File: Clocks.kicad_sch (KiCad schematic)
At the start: 11 parts, among them U3 LMK1C1106A, Y2 O 16,0-JT22CT-A-P-3,3-LF

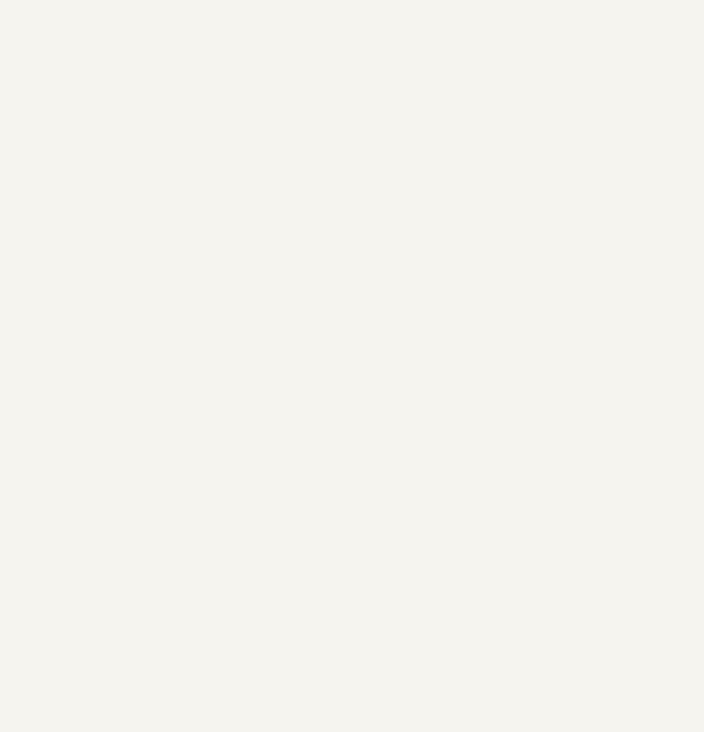
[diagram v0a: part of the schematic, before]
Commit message: Added a thermsistor by the oscillator
For general temperature and for frequency compensation.

Signed-off-by: Corey Minyard <corey@minyard.net>
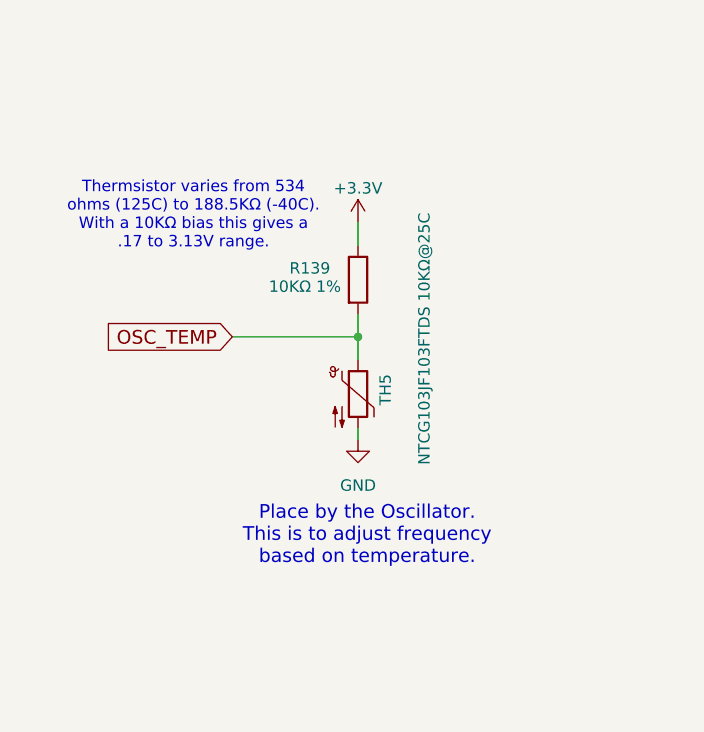
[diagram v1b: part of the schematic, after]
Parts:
- added R139: 10KΩ 1%, Resistor_SMD:R_0402_1005Metric_Pad0.72x0.64mm_HandSolder, symbol Device:R
- added TH5: NTCG103JF103FTDS 10KΩ@25C, Resistor_SMD:R_0402_1005Metric, symbol Device:Thermistor_NTC
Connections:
- net +3.3V: now also R139.1
- net GND: now also TH5.2
- new net OSC_TEMP: R139.2, TH5.1
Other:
- note added: "Place by the Oscillator. This is to adjust frequency based on temperature."
- note added: "Thermsistor varies from 534 ohms (125C) to 188.5KΩ (-40C). With a 10KΩ bias this gives a .17 to 3.13V range."

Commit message: Add a note about a thermal pad on U3
The U3 footprint has a ground pad but the chip itself does not.  Add a
note to put a thermal pad on this chip.

Signed-off-by: Corey Minyard <corey@minyard.net>
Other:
- note added: "This chip does not have a thermal pad on the chip, but does have one in the footprint. Add a thermal pad underneath it to conduct heat from the chip to the board."
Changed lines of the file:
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@@
 		(comment 1 "N5BRG")
+	)
+	(text "This chip does not have a thermal pad on the\nchip, but does have one in the footprint.\nAdd a thermal pad underneath it to conduct\nheat from the chip to the board."
+		(exclude_from_sim no)
+		(at 216.154 149.352 0)
+		(effects
+			(font
+				(size 1.524 1.524)
+			)
+		)
 	)
 	(text "Thermsistor varies from 534\nohms (125C) to 188.5KΩ (-40C).\nWith a 10KΩ bias this gives a\n.17 to 3.13V range."
@@
 	(text "AX5043s have capacitive termination\nat the end of the clocks per their\ndata sheet.  Only need series\ntermination on the CPU clock."
 		(exclude_from_sim no)
-		(at 248.412 134.874 0)
+		(at 285.242 111.506 0)
 		(effects
 			(font

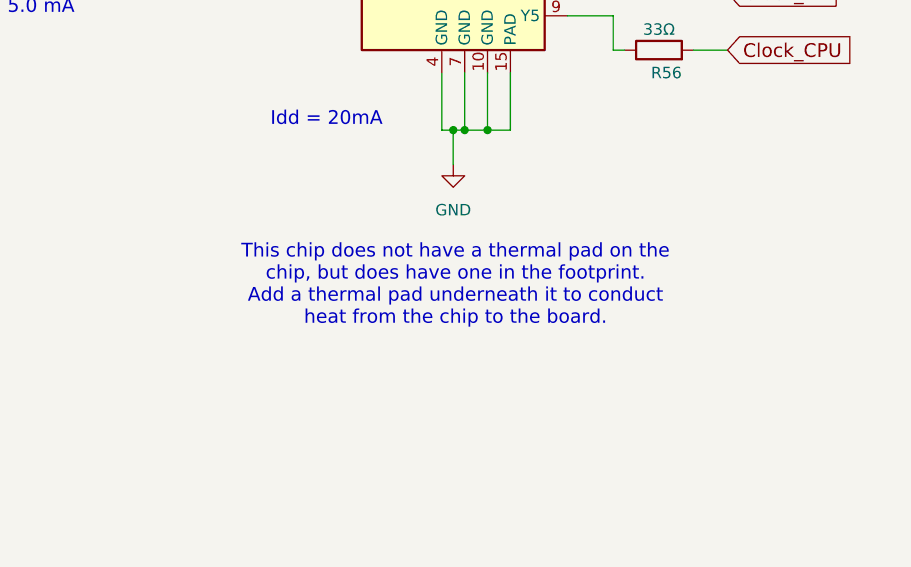
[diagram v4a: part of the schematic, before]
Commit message: Change thermal pads to just be solder contact with the chip
Thermal pads add manufacturing issues and outgassing questions.  I think
the original intent for the clock chip was just to have solder there in
contact with the chip.

So update for that.  This required moving some vias around under the
CPU, but it was doable.

Signed-off-by: Corey Minyard <corey@minyard.net>
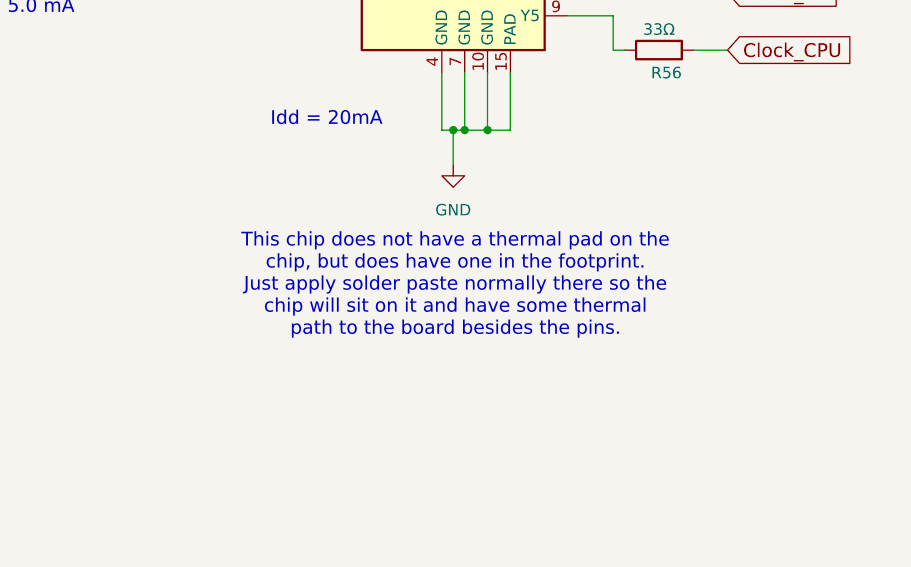
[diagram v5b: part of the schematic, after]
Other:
- note added: "This chip does not have a thermal pad on the chip, but does have one in the footprint. Just apply solder paste normally there so the chip will sit on it and have some thermal path to the board besides the pins."
- note removed: "This chip does not have a thermal pad on the chip, but does have one in the footprint. Add a thermal pad underneath it to conduct heat from the chip to the board."
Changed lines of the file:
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@@
 		(comment 1 "N5BRG")
 	)
-	(text "This chip does not have a thermal pad on the\nchip, but does have one in the footprint.\nAdd a thermal pad underneath it to conduct\nheat from the chip to the board."
+	(text "This chip does not have a thermal pad on the\nchip, but does have one in the footprint.\nJust apply solder paste normally there so the\nchip will sit on it and have some thermal\npath to the board besides the pins."
 		(exclude_from_sim no)
 		(at 216.154 149.352 0)

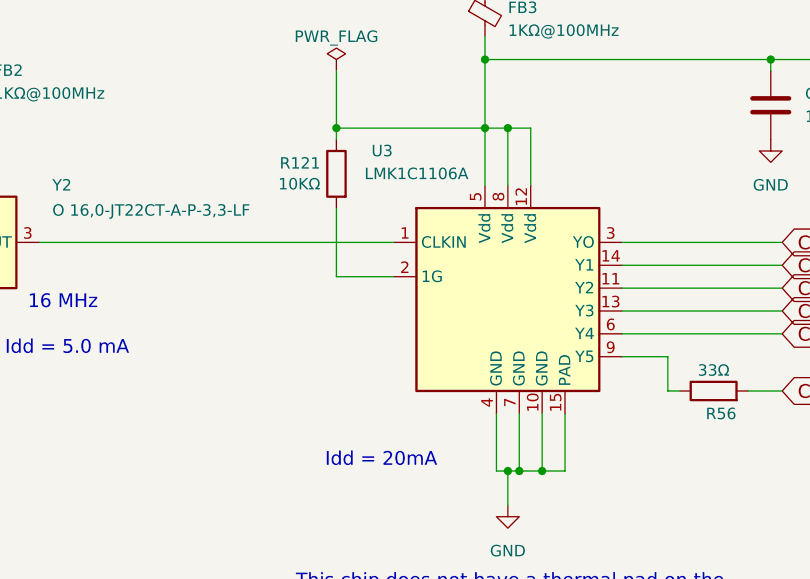
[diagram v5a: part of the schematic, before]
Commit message: Change the LMK1C1106A to a LMK1C1106-Q1
Switch to an automotive part with wider temp range.

Signed-off-by: Corey Minyard <corey@minyard.net>
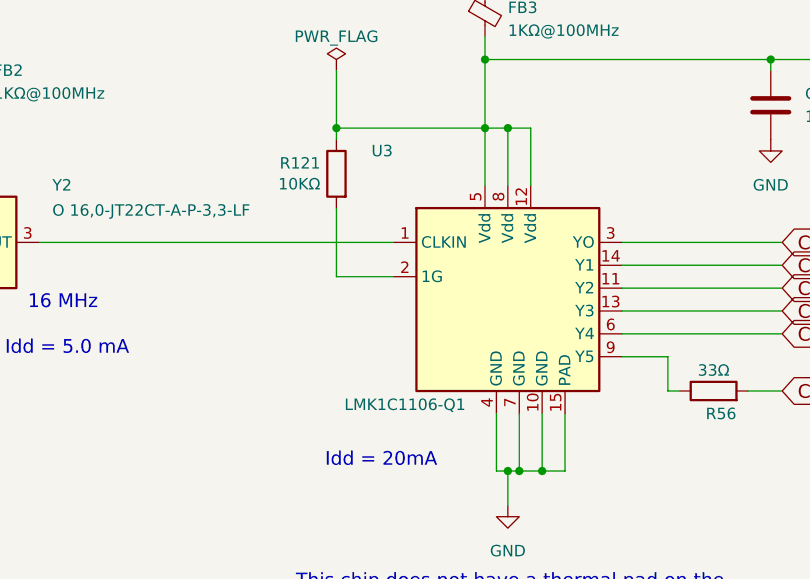
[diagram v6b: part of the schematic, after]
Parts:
- U3: value LMK1C1106A -> LMK1C1106-Q1
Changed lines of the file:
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@@
 			)
 		)
-		(property "Value" "LMK1C1106A"
-			(at 205.74 99.06 0)
+		(property "Value" "LMK1C1106-Q1"
+			(at 204.47 124.714 0)
 			(effects
 				(font
